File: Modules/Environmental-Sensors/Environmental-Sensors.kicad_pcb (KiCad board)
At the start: 2 copper layers, 20.2 x 18 mm, 17 parts, among them J1 Conn_01x04, U1 CCS811, U2 ENS210, U3 BMP280

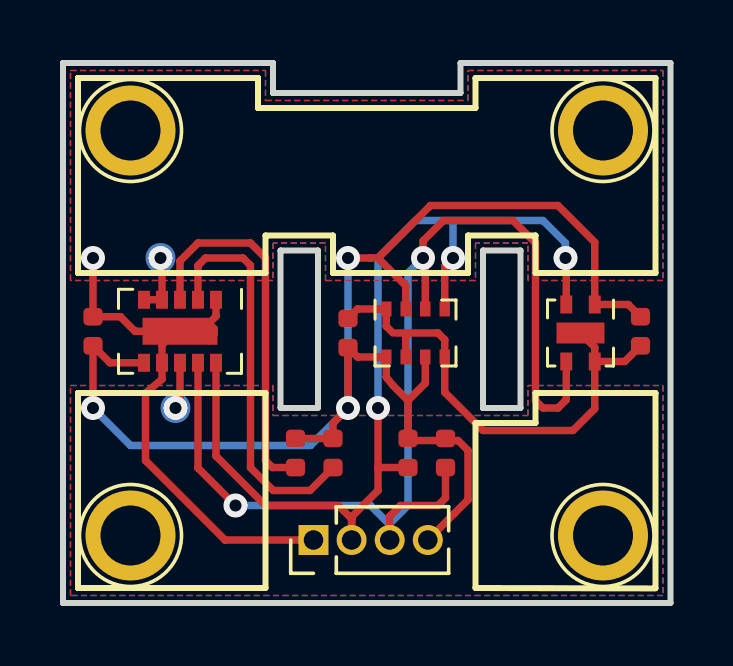
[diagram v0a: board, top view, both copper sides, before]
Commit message: Added version 1.2.0 of environmental sensors board.
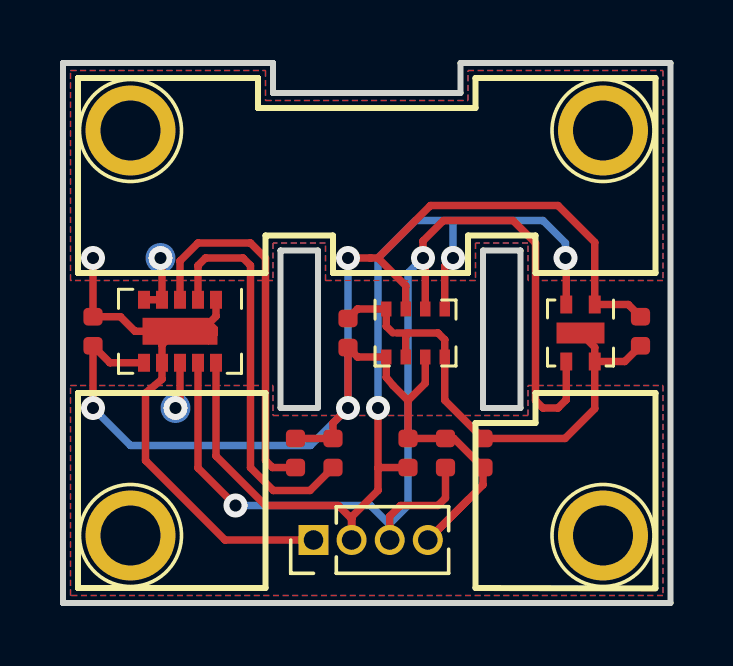
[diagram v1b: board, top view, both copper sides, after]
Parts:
- removed the C3 at (109.2, 79.7)
- added C2: 100nF, Capacitor_SMD:C_0402_1005Metric, F.Cu at (122.2, 83.8)
- added C4: 100nF, Capacitor_SMD:C_0402_1005Metric, F.Cu at (109.2, 79.7)
- C1: value 100nF -> 4.7µF
- U1: footprint Package_LGA:AMS_LGA-10-1EP_2.7x4mm_P0.6mm-2 -> Package_LGA2:AMS_LGA-10-1EP_2.7x4mm_P0.6mm
- renumbered C2 to C3
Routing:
- net +3V3: track 50.3 -> 52.6 mm
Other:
- board text added: "BasilFX 08/2018 V1.2.0"
- board text removed: "BasilFX 08/2018 V1.1.0"
